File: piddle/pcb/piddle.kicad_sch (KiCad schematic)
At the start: 32 parts, among them J1 Conn_01x03_Socket, J10 Conn_01x03_Socket, J2 Conn_01x03_Socket, J3 Conn_01x03_Socket, J4 Conn_01x03_Socket, J5 Conn_01x03_Socket, J6 Conn_01x03_Socket, J7 Conn_01x03_Socket, J8 Conn_01x03_Socket, J9 Conn_01x03_Socket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

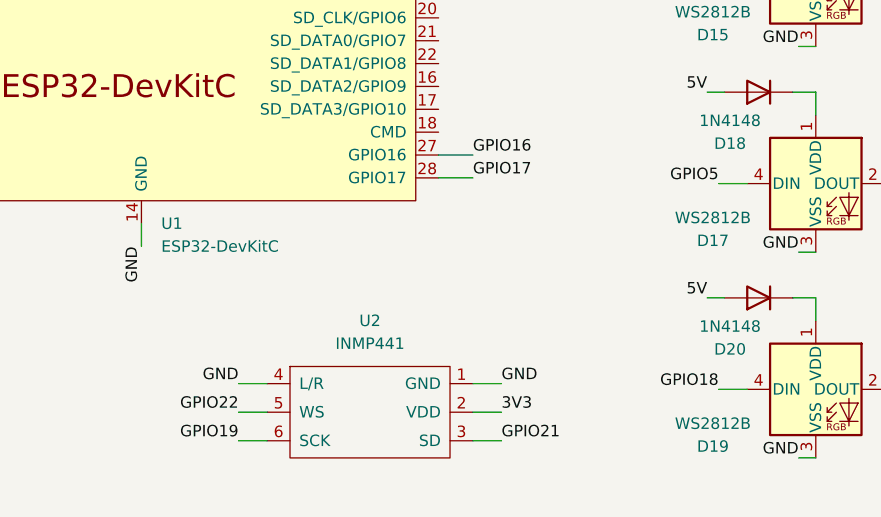
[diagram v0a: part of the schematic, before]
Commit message: Less tangled GPIO
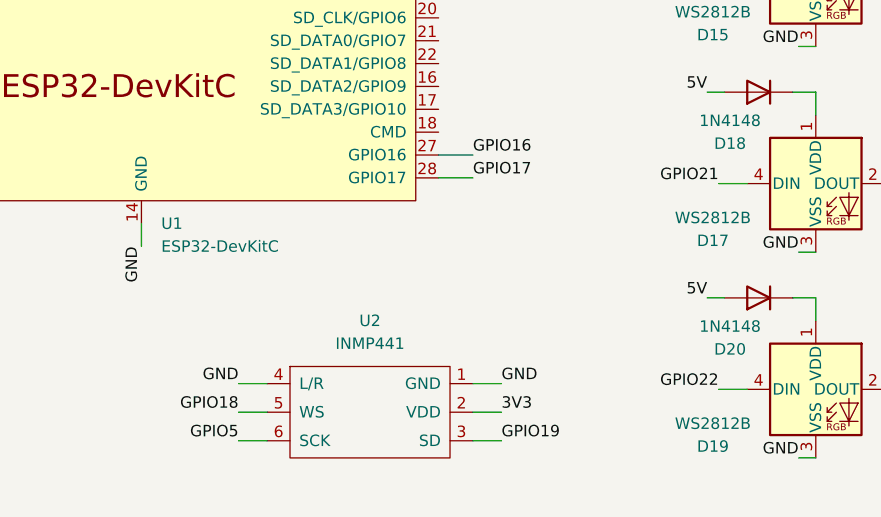
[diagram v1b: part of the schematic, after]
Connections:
- net GPIO18: now also U2.5 (WS); no longer D19.4 (DIN)
- net GPIO19: now also U2.3 (SD); no longer U2.6 (SCK)
- net GPIO21: now also D17.4 (DIN); no longer U2.3 (SD)
- net GPIO22: now also D19.4 (DIN); no longer U2.5 (WS)
- net GPIO5: now also U2.6 (SCK); no longer D17.4 (DIN)
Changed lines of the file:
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@@
     (effects (font (size 1.27 1.27)) (justify left bottom))
   )
-  (label "GPIO18" (at 203.835 139.065 180) (fields_autoplaced)
+  (label "GPIO22" (at 203.835 139.065 180) (fields_autoplaced)
     (effects (font (size 1.27 1.27)) (justify right bottom))
   )
@@
     (effects (font (size 1.27 1.27)) (justify right bottom))
   )
-  (label "GPIO5" (at 203.835 116.205 180) (fields_autoplaced)
+  (label "GPIO21" (at 203.835 116.205 180) (fields_autoplaced)
     (effects (font (size 1.27 1.27)) (justify right bottom))
   )
@@
     (effects (font (size 1.27 1.27)) (justify right bottom))
   )
-  (label "GPIO19" (at 150.495 144.78 180) (fields_autoplaced)
+  (label "GPIO5" (at 150.495 144.78 180) (fields_autoplaced)
     (effects (font (size 1.27 1.27)) (justify right bottom))
   )
@@
     (effects (font (size 1.27 1.27)) (justify left bottom))
   )
-  (label "GPIO22" (at 150.495 141.605 180) (fields_autoplaced)
+  (label "GPIO18" (at 150.495 141.605 180) (fields_autoplaced)
     (effects (font (size 1.27 1.27)) (justify right bottom))
   )
-  (label "GPIO21" (at 179.705 144.78 0) (fields_autoplaced)
+  (label "GPIO19" (at 179.705 144.78 0) (fields_autoplaced)
     (effects (font (size 1.27 1.27)) (justify left bottom))
   )

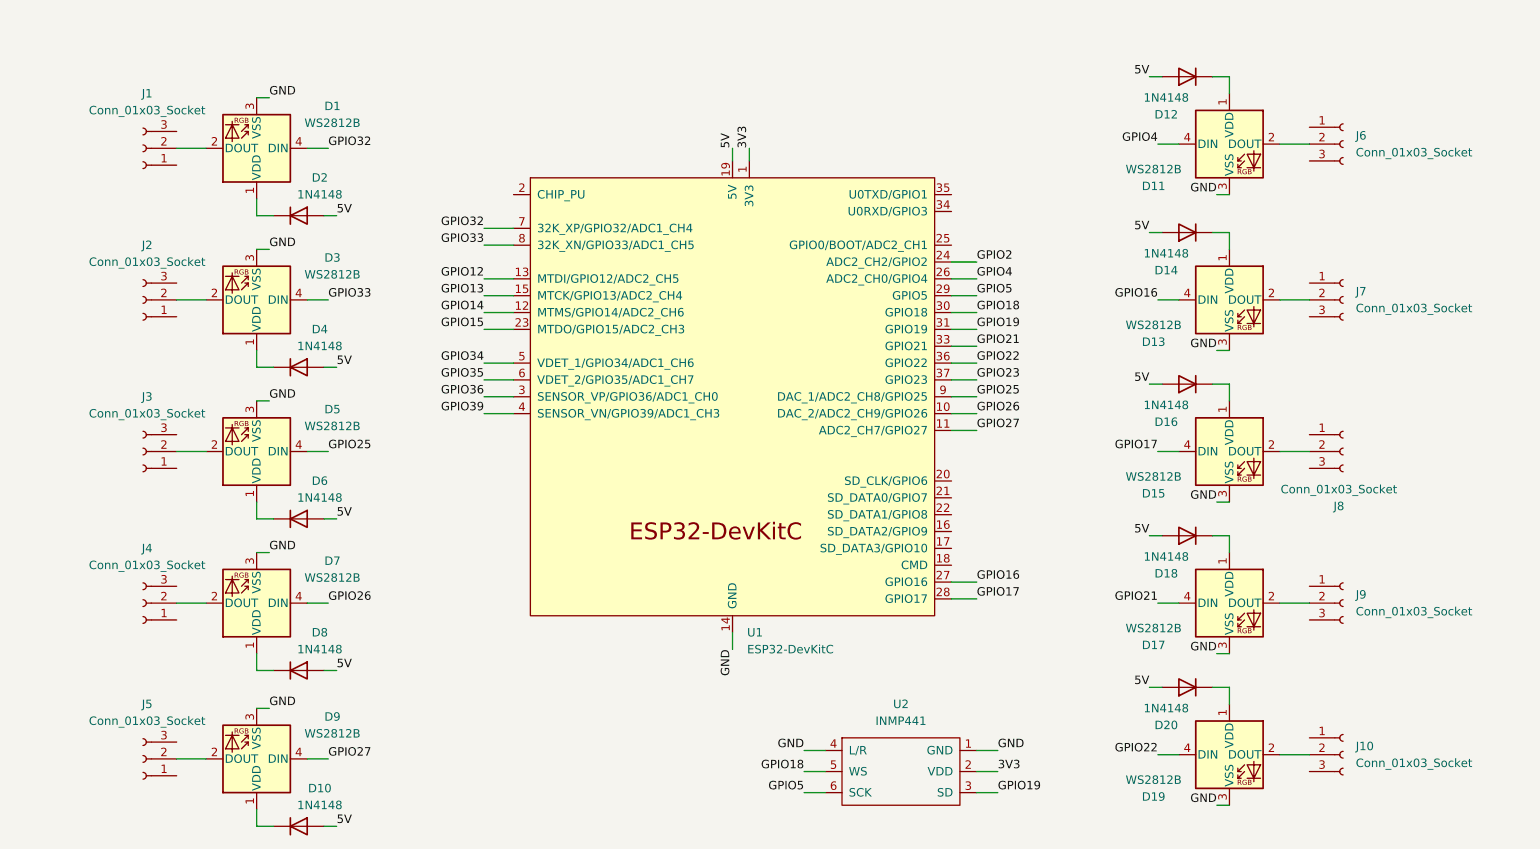
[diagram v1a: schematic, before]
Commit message: Add resistors for each data line
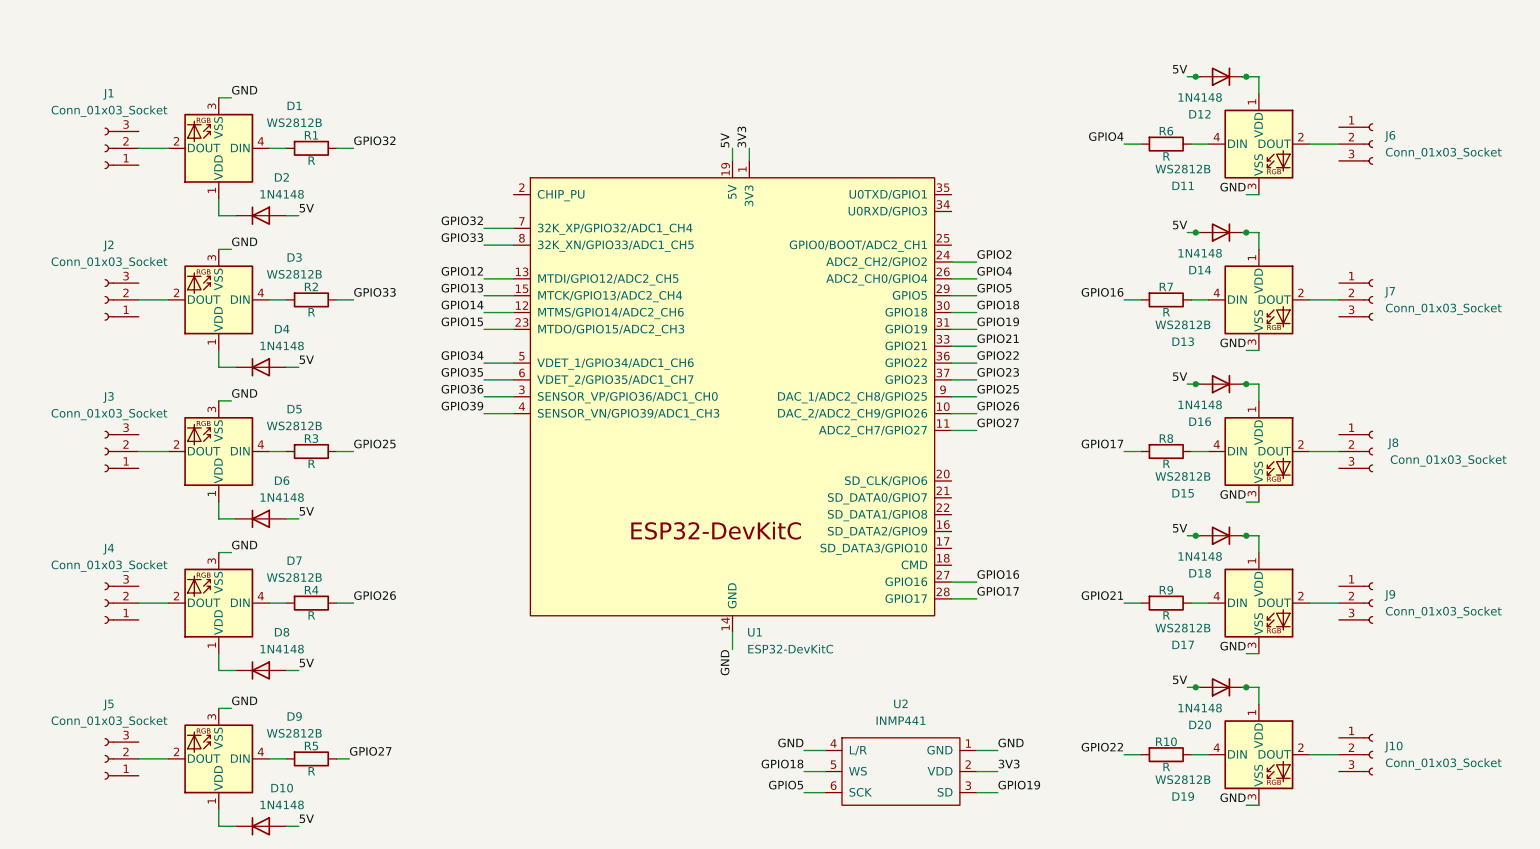
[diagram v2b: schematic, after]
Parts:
- added R1, R10, R2, R3, R4, R5, R6, R7, R8, R9: R, Resistor_THT:R_Axial_DIN0204_L3.6mm_D1.6mm_P5.08mm_Horizontal, symbol Device:R
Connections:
- net GPIO16: now also R7.2; no longer D13.4 (DIN)
- net GPIO17: now also R8.2; no longer D15.4 (DIN)
- net GPIO21: now also R9.2; no longer D17.4 (DIN)
- net GPIO22: now also R10.2; no longer D19.4 (DIN)
- net GPIO25: now also R3.1; no longer D5.4 (DIN)
- net GPIO26: now also R4.1; no longer D7.4 (DIN)
- net GPIO27: now also R5.1; no longer D9.4 (DIN)
- net GPIO32: now also R1.1; no longer D1.4 (DIN)
- net GPIO33: now also R2.1; no longer D3.4 (DIN)
- net GPIO4: now also R6.2; no longer D11.4 (DIN)
- new net: D19.4 (DIN), R10.1
- new net: D1.4 (DIN), R1.2
- new net: D5.4 (DIN), R3.2
- new net: D7.4 (DIN), R4.2
- new net: D11.4 (DIN), R6.1
- new net: D13.4 (DIN), R7.1
- new net: D17.4 (DIN), R9.1
- new net: D9.4 (DIN), R5.2
- new net: D15.4 (DIN), R8.1
- new net: D3.4 (DIN), R2.2
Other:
- moved on the sheet: D1, D10, D11, D12, D13, D14, D15, D16, D17, D18, D19, D2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

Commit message: Add comments
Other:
- company: (none) -> Brandon Skari
- title: (none) -> Phonic Bloom
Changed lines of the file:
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@@
 (kicad_sch (version 20230121) (generator eeschema)
   (paper "A4")
+  (title_block
+    (title "Phonic Bloom")
+    (date "2024-12-21")
+    (rev "1")
+    (company "Brandon Skari")
+    (comment 1 "https://github.com/bskari/apogaea/piddle/")
+  )
   (junction (at 217.17 106.045) (diameter 0) (color 0 0 0 0)
   )

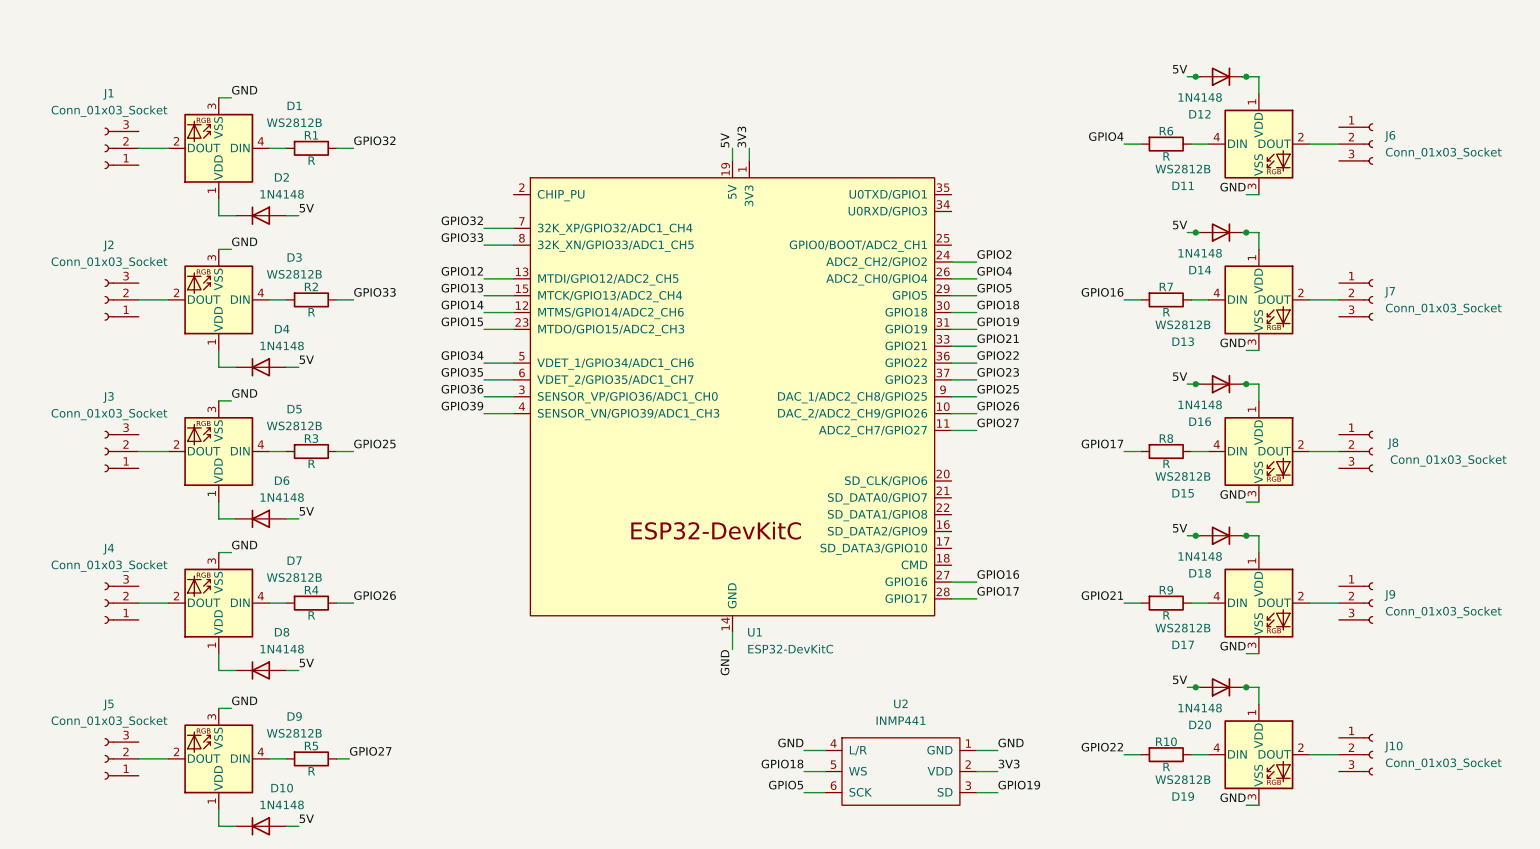
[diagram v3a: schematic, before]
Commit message: Fix power nets
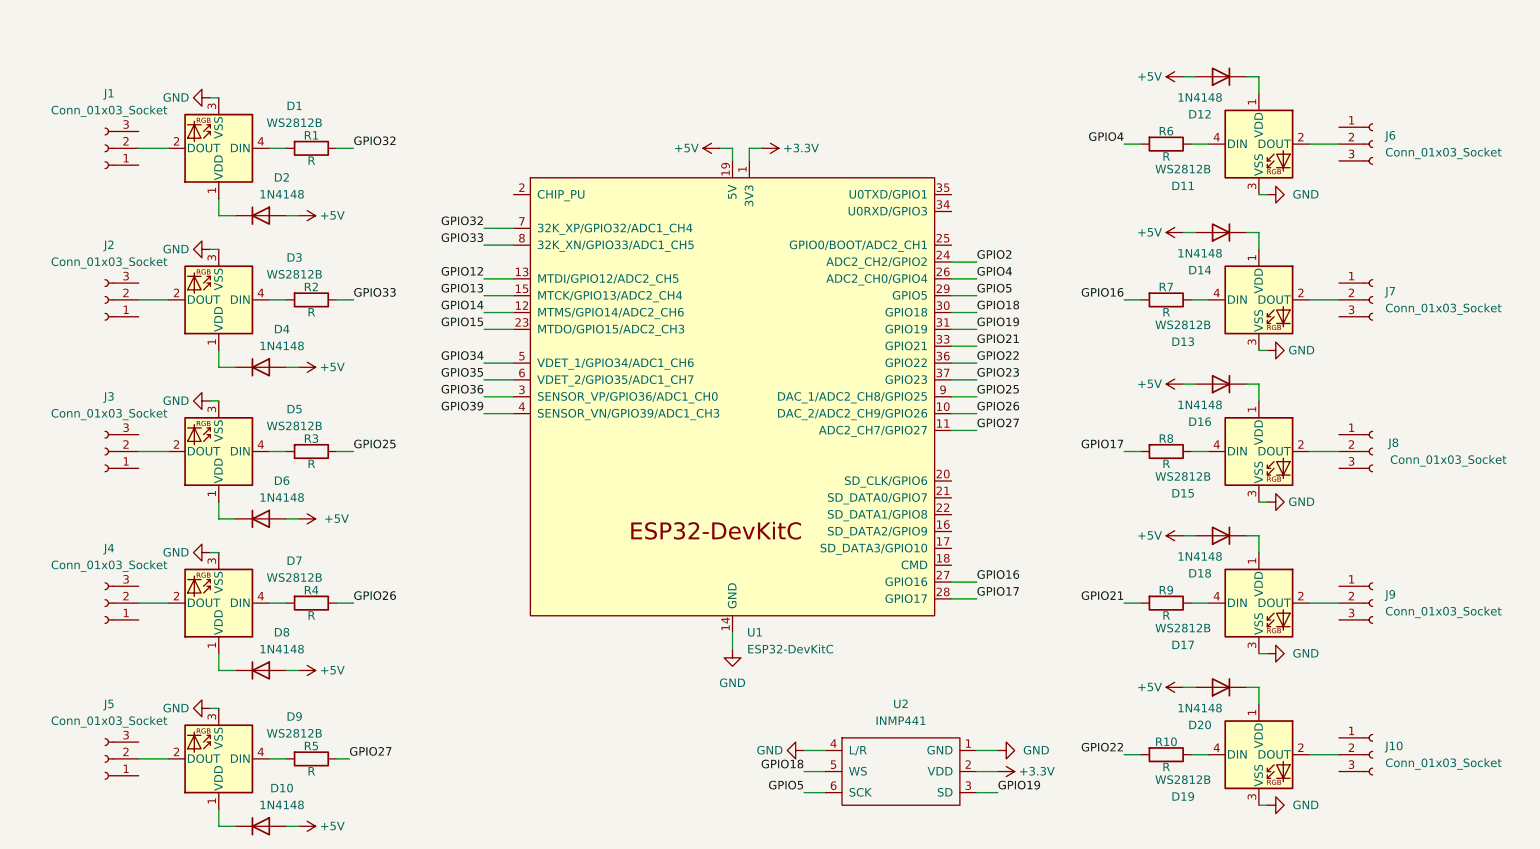
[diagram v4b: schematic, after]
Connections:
- net 3V3 renamed +3.3V
- net 5V renamed +5V

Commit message: Grounds for LED strips
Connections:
- net GND: now also J1.1 (Pin_1), J10.1 (Pin_1), J2.1 (Pin_1), J3.1 (Pin_1), J4.1 (Pin_1), J5.1 (Pin_1), J6.1 (Pin_1), J7.1 (Pin_1), J8.1 (Pin_1), J9.1 (Pin_1)

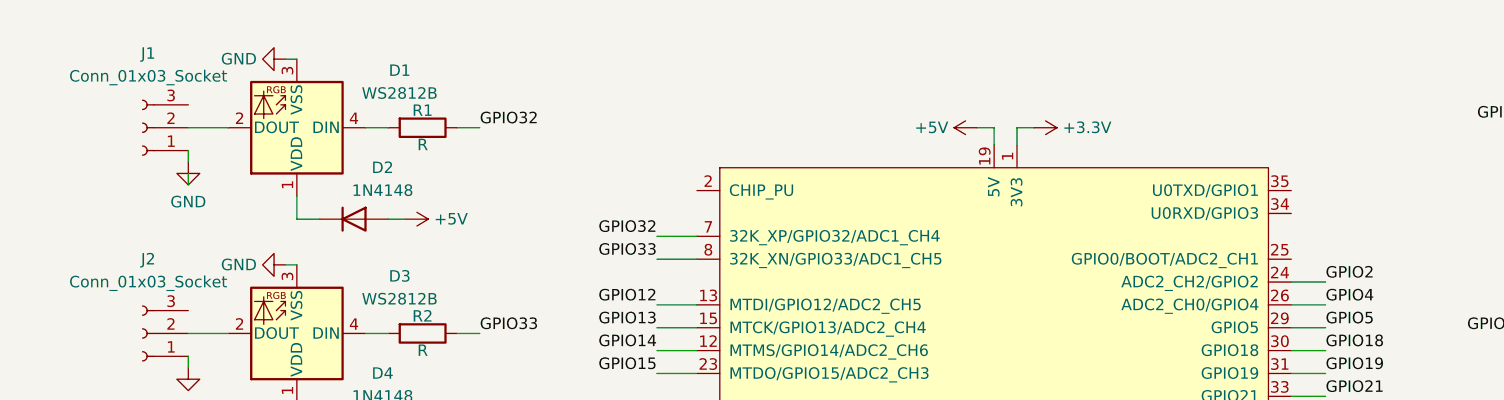
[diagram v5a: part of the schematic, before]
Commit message: Add power connectors
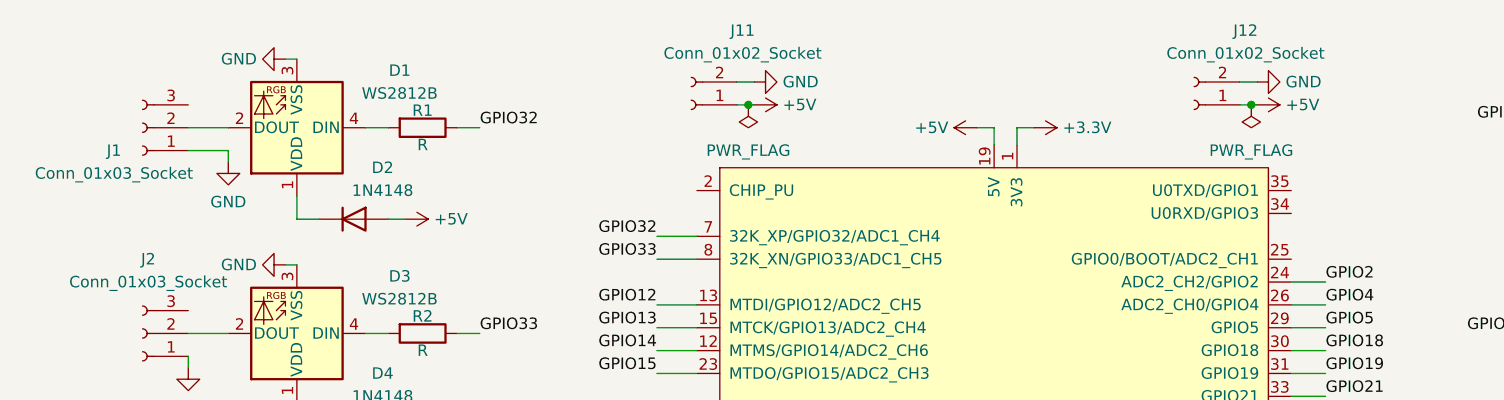
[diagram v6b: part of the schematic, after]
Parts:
- added J11, J12: Conn_01x02_Socket, Connector_JST:JST_PH_S2B-PH-K_1x02_P2.00mm_Horizontal, symbol Connector:Conn_01x02_Socket
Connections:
- net +5V: now also J11.1 (Pin_1), J12.1 (Pin_1)
- net GND: now also J11.2 (Pin_2), J12.2 (Pin_2)

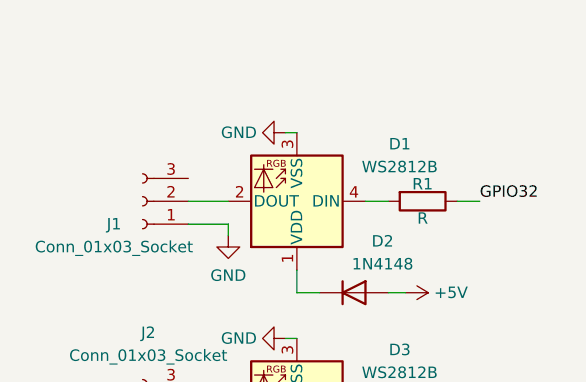
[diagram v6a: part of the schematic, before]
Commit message: Add jumper for powering board from LED strip
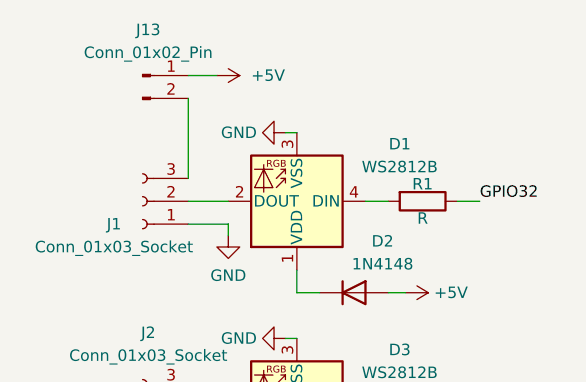
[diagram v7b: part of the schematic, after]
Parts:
- added J13: Conn_01x02_Pin, Connector_PinHeader_2.54mm:PinHeader_1x02_P2.54mm_Vertical, symbol Connector:Conn_01x02_Pin
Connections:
- net +5V: now also J13.1 (Pin_1)
- net at J1.3 (Pin_3): now also J13.2 (Pin_2)
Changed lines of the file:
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@@
+    (stroke (width 0) (type default))
+  )
+  (wire (pts (xy 50.165 33.655) (xy 53.34 33.655))
     (stroke (width 0) (type default))
   )
@@
   )
   (wire (pts (xy 102.235 62.23) (xy 106.68 62.23))
+    (stroke (width 0) (type default))
+  )
+  (wire (pts (xy 50.165 36.195) (xy 50.165 45.085))
     (stroke (width 0) (type default))
   )
@@
         (path "/08f3e99d-6a74-4a56-a078-a6f7466dafc2"
           (reference "J4") (unit 1)
+        )
+      )
+    )
+  )
+  (symbol (lib_id "power:+5V") (at 53.34 33.655 270) (unit 1)
+    (in_bom yes) (on_board yes) (dnp no) (fields_autoplaced)
+    (property "Reference" "#PWR012" (at 49.53 33.655 0)
+      (effects (font (size 1.27 1.27)) hide)
+    )
+    (property "Value" "+5V" (at 57.15 33.655 90)
+      (effects (font (size 1.27 1.27)) (justify left))
+    )
+    (property "Footprint" "" (at 53.34 33.655 0)
+      (effects (font (size 1.27 1.27)) hide)
+    )
+    (property "Datasheet" "" (at 53.34 33.655 0)
+      (effects (font (size 1.27 1.27)) hide)
+    )
+    (pin "1")
+    (instances
+      (project "piddle"
+        (path "/08f3e99d-6a74-4a56-a078-a6f7466dafc2"
+          (reference "#PWR012") (unit 1)
         )
       )
@@
         )
       )
+    )
+  )
+  (symbol (lib_id "Connector:Conn_01x02_Pin") (at 45.085 33.655 0) (unit 1)
+    (in_bom yes) (on_board yes) (dnp no) (fields_autoplaced)
+    (property "Reference" "J13" (at 45.72 28.575 0)
+      (effects (font (size 1.27 1.27)))
+    )
+    (property "Value" "Conn_01x02_Pin" (at 45.72 31.115 0)
+      (effects (font (size 1.27 1.27)))
+    )
+    (property "Footprint" "Connector_PinHeader_2.54mm:PinHeader_1x02_P2.54mm_Vertical" (at 45.085 33.655 0)
+      (effects (font (size 1.27 1.27)) hide)
+    )
+    (property "Datasheet" "~" (at 45.085 33.655 0)
+      (effects (font (size 1.27 1.27)) hide)
+    )
+    (pin "2")
+    (pin "1")
+    (instances
+      (project "piddle"
+        (path "/08f3e99d-6a74-4a56-a078-a6f7466dafc2"
+          (reference "J13") (unit 1)
+        )
+      )
